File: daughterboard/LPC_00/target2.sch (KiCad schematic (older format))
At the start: 27 parts, among them U2 LPC55S69JBD64K

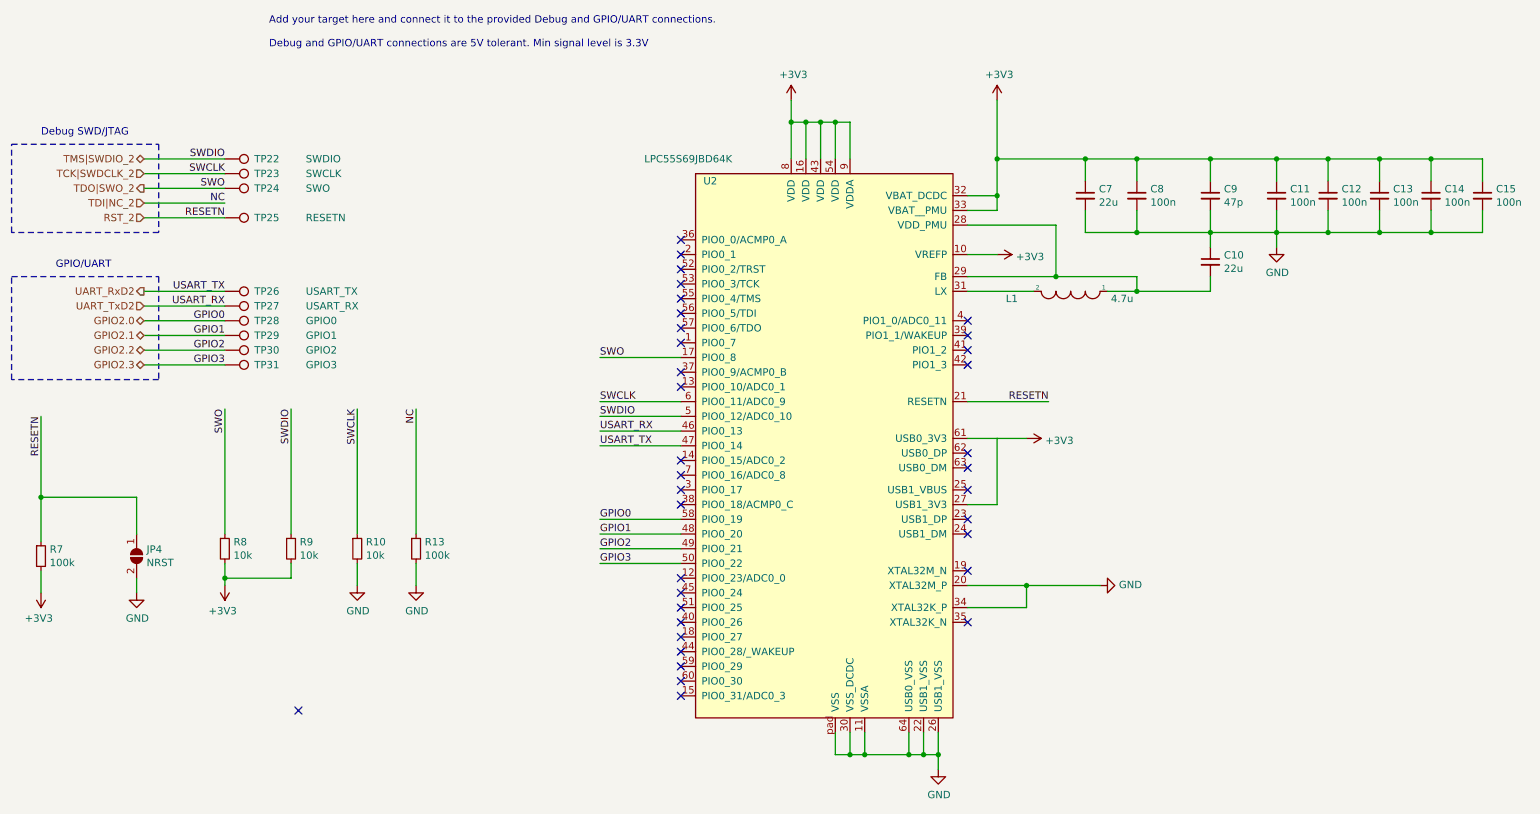
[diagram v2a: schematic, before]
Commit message: sarted with LPC daughterboard layout
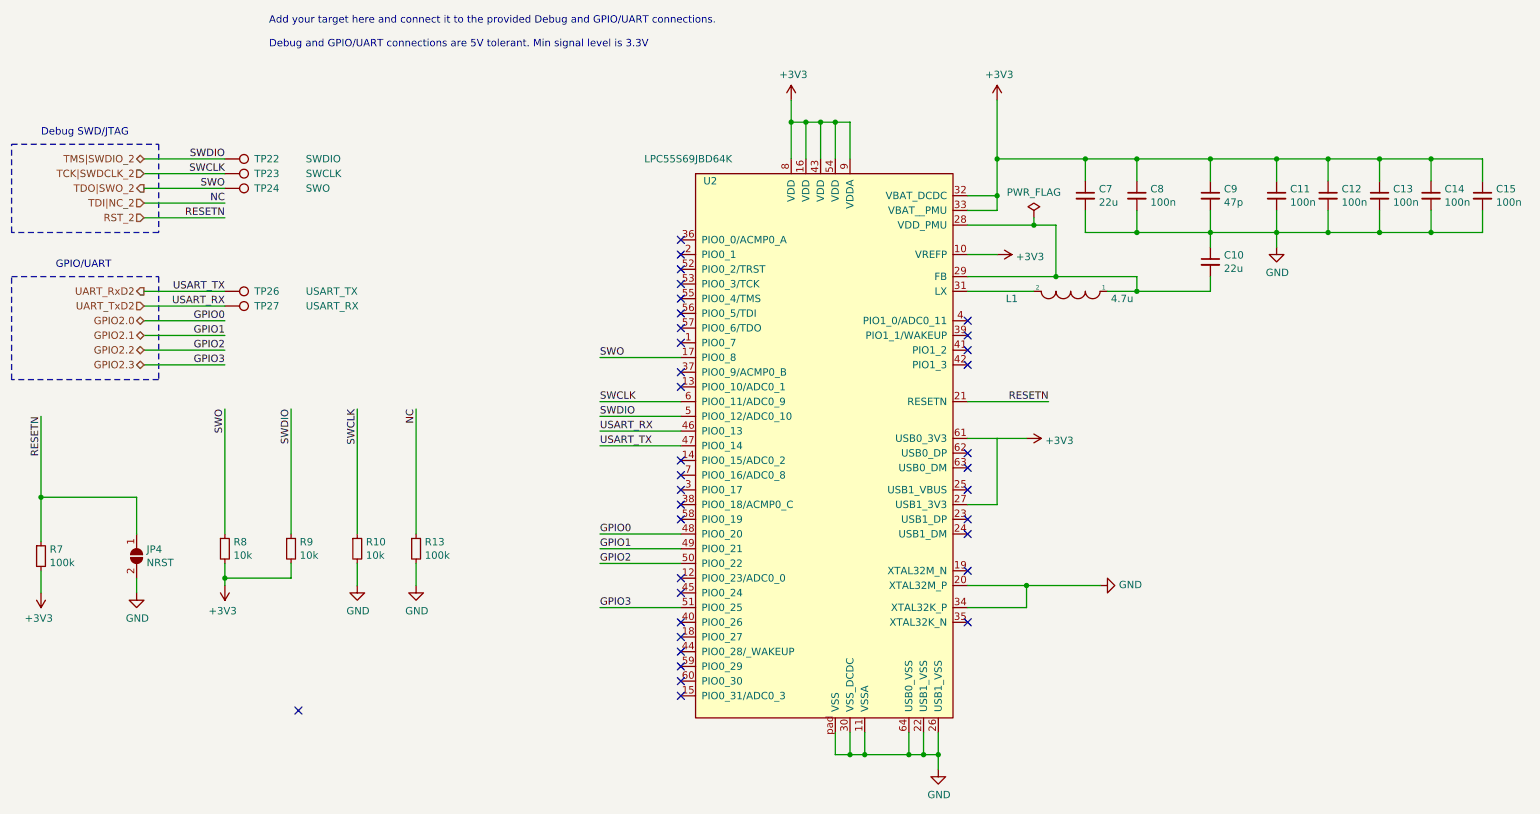
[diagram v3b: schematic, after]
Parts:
- removed TP25: RESETN, symbol Connector:TestPoint
- removed TP28: GPIO0, symbol Connector:TestPoint
- removed TP29: GPIO1, symbol Connector:TestPoint
- removed TP30: GPIO2, symbol Connector:TestPoint
- removed TP31: GPIO3, symbol Connector:TestPoint
- C10, C11, C12, C13, C14, C15, C7, C8, C9: footprint (none) -> Capacitor_SMD:C_0603_1608Metric_Pad1.05x0.95mm_HandSolder
- JP4: footprint (none) -> Jumper:SolderJumper-2_P1.3mm_Open_TrianglePad1.0x1.5mm
- L1: footprint (none) -> hive_daughterboard:TYA40204R7M-10; Model (none) -> TYA40204R7M-10
- R10, R13, R7, R8, R9: footprint (none) -> Resistor_SMD:R_0603_1608Metric_Pad1.05x0.95mm_HandSolder
- TP22, TP23, TP24, TP26, TP27: footprint (none) -> TestPoint:TestPoint_Pad_1.0x1.0mm
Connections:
- net GPIO2.0: now also U2.48 (PIO0_20); no longer U2.58 (PIO0_19)
- net GPIO2.1: now also U2.49 (PIO0_21); no longer U2.48 (PIO0_20)
- net GPIO2.2: now also U2.50 (PIO0_22); no longer U2.49 (PIO0_21)
- net GPIO2.3: now also U2.51 (PIO0_25); no longer U2.50 (PIO0_22)
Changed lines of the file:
@@
 F 0 "L1" H 8350 2650 50  0000 C CNN
 F 1 "4.7u" H 7600 2650 50  0000 C CNN
-F 2 "" H 7950 2600 50  0001 C CNN
+F 2 "hive_daughterboard:TYA40204R7M-10" H 7950 2600 50  0001 C CNN
 F 3 "~" H 7950 2600 50  0001 C CNN
+F 4 "TYA40204R7M-10" H 7950 2600 50  0001 C CNN "Model"
 	1    7950 2600
 	-1   0    0    1
@@
 F 0 "C10" H 8992 2446 50  0000 L CNN
 F 1 "22u" H 8992 2355 50  0000 L CNN
-F 2 "" H 8900 2400 50  0001 C CNN
+F 2 "Capacitor_SMD:C_0603_1608Metric_Pad1.05x0.95mm_HandSolder" H 8900 2400 50  0001 C CNN
 F 3 "~" H 8900 2400 50  0001 C CNN
 	1    8900 2400
@@
 F 0 "C11" H 9442 1996 50  0000 L CNN
 F 1 "100n" H 9442 1905 50  0000 L CNN
-F 2 "" H 9350 1950 50  0001 C CNN
+F 2 "Capacitor_SMD:C_0603_1608Metric_Pad1.05x0.95mm_HandSolder" H 9350 1950 50  0001 C CNN
 F 3 "~" H 9350 1950 50  0001 C CNN
 	1    9350 1950
@@
 F 0 "C12" H 9792 1996 50  0000 L CNN
 F 1 "100n" H 9792 1905 50  0000 L CNN
-F 2 "" H 9700 1950 50  0001 C CNN
+F 2 "Capacitor_SMD:C_0603_1608Metric_Pad1.05x0.95mm_HandSolder" H 9700 1950 50  0001 C CNN
 F 3 "~" H 9700 1950 50  0001 C CNN
 	1    9700 1950
@@
 F 0 "C13" H 10142 1996 50  0000 L CNN
 F 1 "100n" H 10142 1905 50  0000 L CNN
-F 2 "" H 10050 1950 50  0001 C CNN
+F 2 "Capacitor_SMD:C_0603_1608Metric_Pad1.05x0.95mm_HandSolder" H 10050 1950 50  0001 C CNN
 F 3 "~" H 10050 1950 50  0001 C CNN
 	1    10050 1950
@@
 F 0 "C14" H 10492 1996 50  0000 L CNN
 F 1 "100n" H 10492 1905 50  0000 L CNN
-F 2 "" H 10400 1950 50  0001 C CNN
+F 2 "Capacitor_SMD:C_0603_1608Metric_Pad1.05x0.95mm_HandSolder" H 10400 1950 50  0001 C CNN
 F 3 "~" H 10400 1950 50  0001 C CNN
 	1    10400 1950
@@
 F 0 "C7" H 8142 1996 50  0000 L CNN
 F 1 "22u" H 8142 1905 50  0000 L CNN
-F 2 "" H 8050 1950 50  0001 C CNN
+F 2 "Capacitor_SMD:C_0603_1608Metric_Pad1.05x0.95mm_HandSolder" H 8050 1950 50  0001 C CNN
 F 3 "~" H 8050 1950 50  0001 C CNN
 	1    8050 1950
@@
 F 0 "C9" H 8992 1996 50  0000 L CNN
 F 1 "47p" H 8992 1905 50  0000 L CNN
-F 2 "" H 8900 1950 50  0001 C CNN
+F 2 "Capacitor_SMD:C_0603_1608Metric_Pad1.05x0.95mm_HandSolder" H 8900 1950 50  0001 C CNN
 F 3 "~" H 8900 1950 50  0001 C CNN
 	1    8900 1950
@@
 F 0 "C8" H 8492 1996 50  0000 L CNN
 F 1 "100n" H 8492 1905 50  0000 L CNN
-F 2 "" H 8400 1950 50  0001 C CNN
+F 2 "Capacitor_SMD:C_0603_1608Metric_Pad1.05x0.95mm_HandSolder" H 8400 1950 50  0001 C CNN
 F 3 "~" H 8400 1950 50  0001 C CNN
 	1    8400 1950
@@
 F 0 "C15" H 10842 1996 50  0000 L CNN
 F 1 "100n" H 10842 1905 50  0000 L CNN
-F 2 "" H 10750 1950 50  0001 C CNN
+F 2 "Capacitor_SMD:C_0603_1608Metric_Pad1.05x0.95mm_HandSolder" H 10750 1950 50  0001 C CNN
 F 3 "~" H 10750 1950 50  0001 C CNN
 	1    10750 1950
@@
 F 0 "R7" H 1009 4446 50  0000 L CNN
 F 1 "100k" H 1009 4355 50  0000 L CNN
-F 2 "" H 950 4400 50  0001 C CNN
+F 2 "Resistor_SMD:R_0603_1608Metric_Pad1.05x0.95mm_HandSolder" H 950 4400 50  0001 C CNN
 F 3 "~" H 950 4400 50  0001 C CNN
 	1    950  4400
@@
 F 0 "JP4" V 1554 4468 50  0000 L CNN
 F 1 "NRST" V 1645 4468 50  0000 L CNN
-F 2 "" H 1600 4400 50  0001 C CNN
+F 2 "Jumper:SolderJumper-2_P1.3mm_Open_TrianglePad1.0x1.5mm" H 1600 4400 50  0001 C CNN
 F 3 "~" H 1600 4400 50  0001 C CNN
 	1    1600 4400
@@
 F 0 "R8" H 2259 4396 50  0000 L CNN
 F 1 "10k" H 2259 4305 50  0000 L CNN
-F 2 "" H 2200 4350 50  0001 C CNN
+F 2 "Resistor_SMD:R_0603_1608Metric_Pad1.05x0.95mm_HandSolder" H 2200 4350 50  0001 C CNN
 F 3 "~" H 2200 4350 50  0001 C CNN
 	1    2200 4350
@@
 F 0 "R9" H 2709 4396 50  0000 L CNN
 F 1 "10k" H 2709 4305 50  0000 L CNN
-F 2 "" H 2650 4350 50  0001 C CNN
+F 2 "Resistor_SMD:R_0603_1608Metric_Pad1.05x0.95mm_HandSolder" H 2650 4350 50  0001 C CNN
 F 3 "~" H 2650 4350 50  0001 C CNN
 	1    2650 4350
@@
 F 0 "R10" H 3159 4396 50  0000 L CNN
 F 1 "10k" H 3159 4305 50  0000 L CNN
-F 2 "" H 3100 4350 50  0001 C CNN
+F 2 "Resistor_SMD:R_0603_1608Metric_Pad1.05x0.95mm_HandSolder" H 3100 4350 50  0001 C CNN
 F 3 "~" H 3100 4350 50  0001 C CNN
 	1    3100 4350
@@
 USART_TX
 Wire Wire Line
-	5300 4250 4750 4250
+	5300 4350 4750 4350
+Text Label 4750 4350 0    50   ~ 0
+GPIO1
 Text Label 4750 4250 0    50   ~ 0
-GPIO1
-Wire Wire Line
-	5300 4150 4750 4150
-Text Label 4750 4150 0    50   ~ 0
 GPIO0
+Text Label 4750 4750 0    50   ~ 0
+GPIO3
 Wire Wire Line
 	5300 4450 4750 4450
 Text Label 4750 4450 0    50   ~ 0
-GPIO3
-Wire Wire Line
-	5300 4350 4750 4350
-Text Label 4750 4350 0    50   ~ 0
 GPIO2
 NoConn ~ 5300 2250
@@
 NoConn ~ 5300 4550
 NoConn ~ 5300 4650
-NoConn ~ 5300 4750
+NoConn ~ 5300 4150
 NoConn ~ 5300 4850
 NoConn ~ 5300 4950
@@
 F 0 "R13" H 3559 4396 50  0000 L CNN
 F 1 "100k" H 3559 4305 50  0000 L CNN
-F 2 "" H 3500 4350 50  0001 C CNN
+F 2 "Resistor_SMD:R_0603_1608Metric_Pad1.05x0.95mm_HandSolder" H 3500 4350 50  0001 C CNN
 F 3 "~" H 3500 4350 50  0001 C CNN
 	1    3500 4350
@@
 	3500 3400 3500 4250
 Wire Wire Line
-	7250 2150 7850 2150
+	7250 2150 7700 2150
 $Comp
 L Connector:TestPoint TP22
@@
 F 0 "TP22" V 2200 1900 50  0000 L CNN
 F 1 "SWDIO" V 2200 2250 50  0000 L CNN
-F 2 "" H 2400 1700 50  0001 C CNN
+F 2 "TestPoint:TestPoint_Pad_1.0x1.0mm" H 2400 1700 50  0001 C CNN
 F 3 "~" H 2400 1700 50  0001 C CNN
 	1    2200 1700
@@
 F 0 "TP23" V 2200 2000 50  0000 L CNN
 F 1 "SWCLK" V 2200 2350 50  0000 L CNN
-F 2 "" H 2400 1800 50  0001 C CNN
+F 2 "TestPoint:TestPoint_Pad_1.0x1.0mm" H 2400 1800 50  0001 C CNN
 F 3 "~" H 2400 1800 50  0001 C CNN
 	1    2200 1800
@@
 F 0 "TP24" V 2200 2100 50  0000 L CNN
 F 1 "SWO" V 2200 2450 50  0000 L CNN
-F 2 "" H 2400 1900 50  0001 C CNN
+F 2 "TestPoint:TestPoint_Pad_1.0x1.0mm" H 2400 1900 50  0001 C CNN
 F 3 "~" H 2400 1900 50  0001 C CNN
 	1    2200 1900
-	0    1    1    0
-$EndComp
-$Comp
-L Connector:TestPoint TP25
-U 1 1 6190C6D5
-P 2200 2100
-F 0 "TP25" V 2200 2300 50  0000 L CNN
-F 1 "RESETN" V 2200 2650 50  0000 L CNN
-F 2 "" H 2400 2100 50  0001 C CNN
-F 3 "~" H 2400 2100 50  0001 C CNN
-	1    2200 2100
 	0    1    1    0
 $EndComp
@@
 F 0 "TP26" V 2200 2800 50  0000 L CNN
 F 1 "USART_TX" V 2200 3150 50  0000 L CNN
-F 2 "" H 2400 2600 50  0001 C CNN
+F 2 "TestPoint:TestPoint_Pad_1.0x1.0mm" H 2400 2600 50  0001 C CNN
 F 3 "~" H 2400 2600 50  0001 C CNN
 	1    2200 2600
@@
 F 0 "TP27" V 2200 2900 50  0000 L CNN
 F 1 "USART_RX" V 2200 3250 50  0000 L CNN
-F 2 "" H 2400 2700 50  0001 C CNN
+F 2 "TestPoint:TestPoint_Pad_1.0x1.0mm" H 2400 2700 50  0001 C CNN
 F 3 "~" H 2400 2700 50  0001 C CNN
 	1    2200 2700
@@
 $EndComp
 $Comp
-L Connector:TestPoint TP28
-U 1 1 6190D9F7
-P 2200 2800
-F 0 "TP28" V 2200 3000 50  0000 L CNN
-F 1 "GPIO0" V 2200 3350 50  0000 L CNN
-F 2 "" H 2400 2800 50  0001 C CNN
-F 3 "~" H 2400 2800 50  0001 C CNN
-	1    2200 2800
-	0    1    1    0
-$EndComp
-$Comp
-L Connector:TestPoint TP29
-U 1 1 6190DCED
-P 2200 2900
-F 0 "TP29" V 2200 3100 50  0000 L CNN
-F 1 "GPIO1" V 2200 3450 50  0000 L CNN
-F 2 "" H 2400 2900 50  0001 C CNN
-F 3 "~" H 2400 2900 50  0001 C CNN
-	1    2200 2900
-	0    1    1    0
-$EndComp
-$Comp
-L Connector:TestPoint TP30
-U 1 1 6190E02F
-P 2200 3000
-F 0 "TP30" V 2200 3200 50  0000 L CNN
-F 1 "GPIO2" V 2200 3550 50  0000 L CNN
-F 2 "" H 2400 3000 50  0001 C CNN
-F 3 "~" H 2400 3000 50  0001 C CNN
-	1    2200 3000
-	0    1    1    0
-$EndComp
-$Comp
-L Connector:TestPoint TP31
-U 1 1 6190E301
-P 2200 3100
-F 0 "TP31" V 2200 3300 50  0000 L CNN
-F 1 "GPIO3" V 2200 3650 50  0000 L CNN
-F 2 "" H 2400 3100 50  0001 C CNN
-F 3 "~" H 2400 3100 50  0001 C CNN
-	1    2200 3100
-	0    1    1    0
-$EndComp
+L power:PWR_FLAG #FLG0101
+U 1 1 61933E23
+P 7700 2100
+F 0 "#FLG0101" H 7700 2175 50  0001 C CNN
+F 1 "PWR_FLAG" H 7700 2273 50  0000 C CNN
+F 2 "" H 7700 2100 50  0001 C CNN
+F 3 "~" H 7700 2100 50  0001 C CNN
+	1    7700 2100
+	1    0    0    -1
+$EndComp
+Wire Wire Line
+	7700 2100 7700 2150
+Connection ~ 7700 2150
+Wire Wire Line
+	7700 2150 7850 2150
+Wire Wire Line
+	5300 4750 4750 4750
+Wire Wire Line
+	5300 4250 4750 4250
 $EndSCHEMATC
